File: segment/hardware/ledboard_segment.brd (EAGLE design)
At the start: 21.8 x 22.1 mm, 13 parts, among them J1 ISP, U1 ATMEGA328P_TQFP, Y1 16MHz

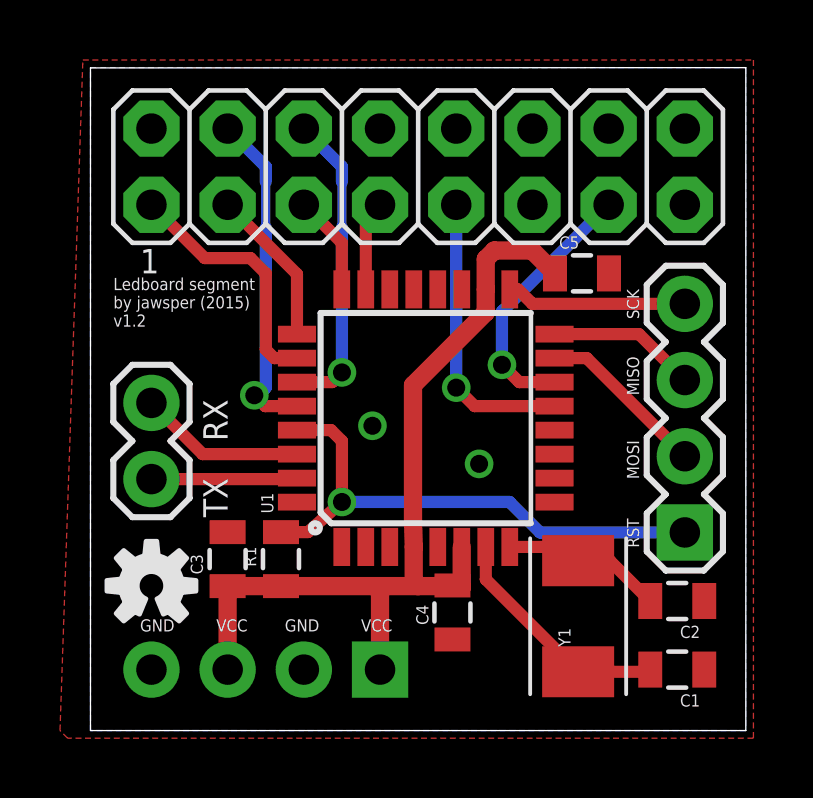
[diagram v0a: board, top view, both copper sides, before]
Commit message: Made board 10 mil smaller + minor tweaks
Some prettification of traces.
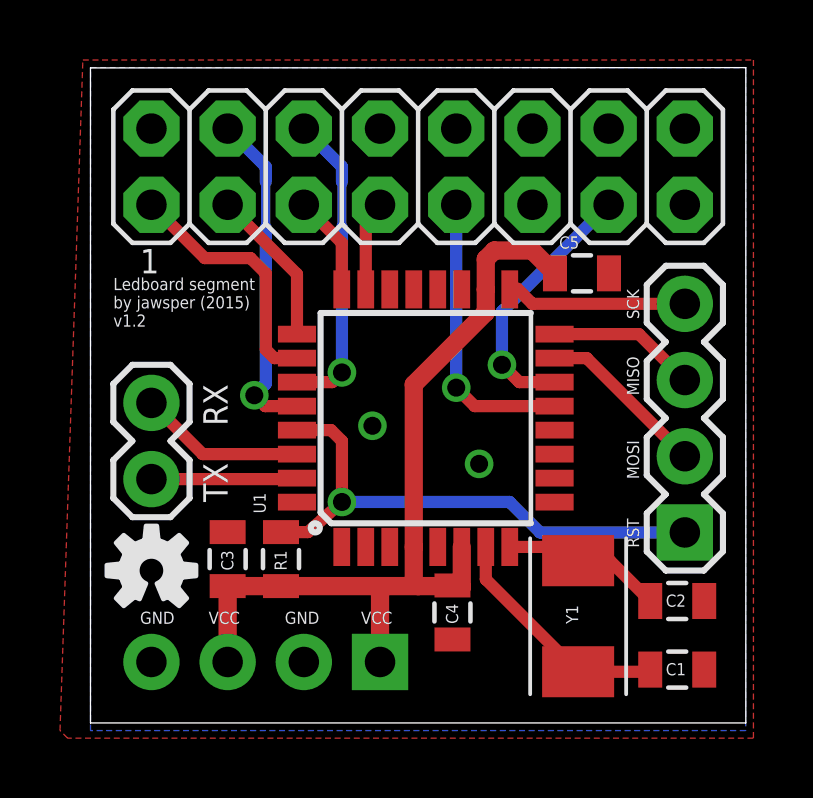
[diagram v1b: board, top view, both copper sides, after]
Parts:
- moved U$2 0.51 mm to (4.32, 59.7)
- moved JP2 0.25 mm to (11.9, 56.6)
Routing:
- net VCC: track 29.5 -> 29.0 mm
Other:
- board size 21.8 x 22.1 mm -> 21.8 x 21.8 mm
